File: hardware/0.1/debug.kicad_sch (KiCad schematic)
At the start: 11 parts, among them J401 JTAG, J402 JTAG, SW401 KMR2

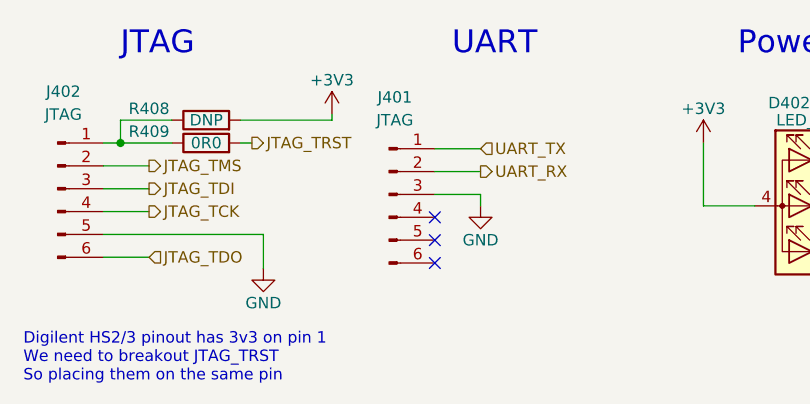
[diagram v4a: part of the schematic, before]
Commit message: usb3 routed less tuning
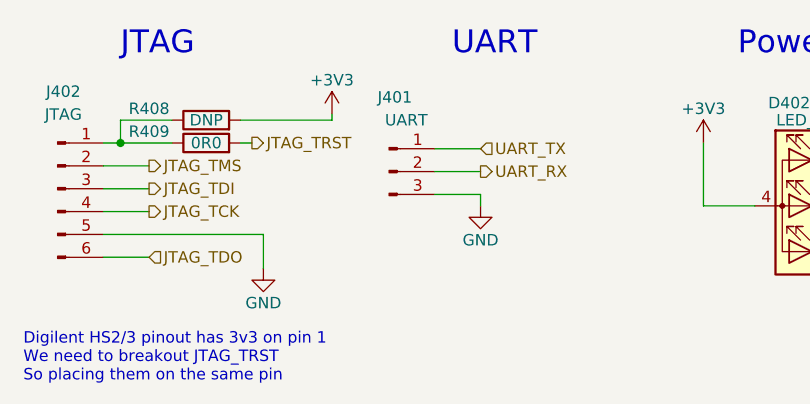
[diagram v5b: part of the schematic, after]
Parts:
- removed J401: JTAG, Connector:Tag-Connect_TC2030-IDC-NL_2x03_P1.27mm_Vertical, symbol Connector:Conn_01x06_Male
- added J401: UART, josh-connectors:3_PIN_THT_Staggered, symbol Connector:Conn_01x03_Male
- J402: footprint Connector:Tag-Connect_TC2030-IDC-NL_2x03_P1.27mm_Vertical -> josh-connectors:6_PIN_THT_Staggered
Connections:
- net GND: now also J401.3 (Pin_3)
- net UART_RX: now also J401.2 (Pin_2)
- net UART_TX: now also J401.1 (Pin_1)
- no-connect marks 3 -> 0
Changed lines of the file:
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@@
   (junction (at 74.295 98.425) (diameter 0) (color 0 0 0 0)
   )
-  (no_connect (at 160.02 98.425))
-  (no_connect (at 160.02 100.965))
-  (no_connect (at 160.02 103.505))
   (wire (pts (xy 128.27 102.87) (xy 123.19 102.87))
     (stroke (width 0) (type default) (color 0 0 0 0))
@@
     (property "Reference" "J402" (id 0) (at 118.745 84.455 0))
     (property "Value" "JTAG" (id 1) (at 118.745 86.995 0))
-    (property "Footprint" "Connector:Tag-Connect_TC2030-IDC-NL_2x03_P1.27mm_Vertical" (id 2) (at 118.11 95.25 0)
+    (property "Footprint" "josh-connectors:6_PIN_THT_Staggered" (id 2) (at 118.11 95.25 0)
       (effects (font (size 1.27 1.27)) hide)
     )
@@
     (pin "1")
   )
+  (symbol (lib_id "Connector:Conn_01x03_Male") (at 154.94 93.345 0) (unit 1)
+    (in_bom yes) (on_board yes)
+    (property "Reference" "J401" (id 0) (at 155.575 85.09 0))
+    (property "Value" "UART" (id 1) (at 156.845 87.63 0))
+    (property "Footprint" "josh-connectors:3_PIN_THT_Staggered" (id 2) (at 154.94 93.345 0)
+      (effects (font (size 1.27 1.27)) hide)
+    )
+    (property "Datasheet" "~" (id 3) (at 154.94 93.345 0)
+      (effects (font (size 1.27 1.27)) hide)
+    )
+    (pin "1")
+    (pin "2")
+    (pin "3")
+  )
   (symbol (lib_id "Device:R") (at 134.62 90.17 90) (unit 1)
     (in_bom yes) (on_board yes)
@@
     (pin "2")
   )
-  (symbol (lib_id "Connector:Conn_01x06_Male") (at 154.94 95.885 0) (unit 1)
-    (in_bom no) (on_board yes) (fields_autoplaced)
-    (property "Reference" "J401" (id 0) (at 155.575 85.09 0))
-    (property "Value" "JTAG" (id 1) (at 155.575 87.63 0))
-    (property "Footprint" "Connector:Tag-Connect_TC2030-IDC-NL_2x03_P1.27mm_Vertical" (id 2) (at 154.94 95.885 0)
-      (effects (font (size 1.27 1.27)) hide)
-    )
-    (property "Datasheet" "~" (id 3) (at 154.94 95.885 0)
-      (effects (font (size 1.27 1.27)) hide)
-    )
-    (pin "1")
-    (pin "2")
-    (pin "3")
-    (pin "4")
-    (pin "5")
-    (pin "6")
-  )
   (symbol (lib_id "power:GND") (at 76.835 107.95 0) (unit 1)

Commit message: wip, switchers todo
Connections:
- net GND: now also J401.1 (Pin_1); no longer J401.3 (Pin_3)
- net UART_TX: now also J401.3 (Pin_3); no longer J401.1 (Pin_1)
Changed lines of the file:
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@@
     (pin "1")
   )
-  (symbol (lib_id "Connector:Conn_01x03_Male") (at 154.94 93.345 0) (unit 1)
+  (symbol (lib_id "Connector:Conn_01x03_Male") (at 154.94 93.345 0) (mirror x) (unit 1)
     (in_bom yes) (on_board yes)
-    (property "Reference" "J401" (id 0) (at 155.575 85.09 0))
+    (property "Reference" "J401" (id 0) (at 156.845 85.725 0))
     (property "Value" "UART" (id 1) (at 156.845 87.63 0))
     (property "Footprint" "josh-connectors:3_PIN_THT_Staggered" (id 2) (at 154.94 93.345 0)

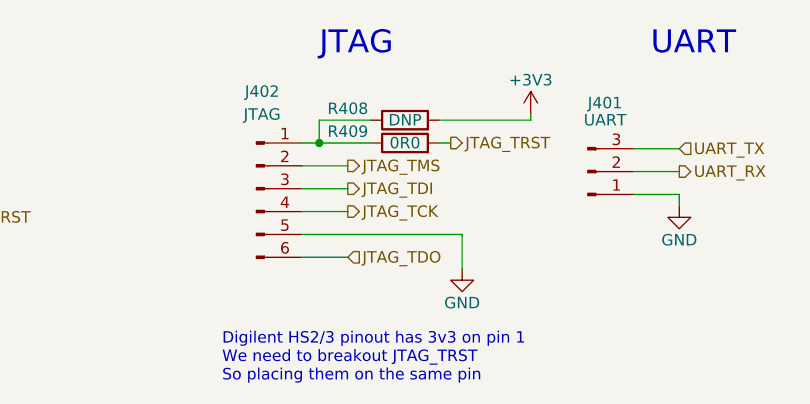
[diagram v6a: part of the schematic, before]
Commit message: erc = drc = 0, fixup BOM
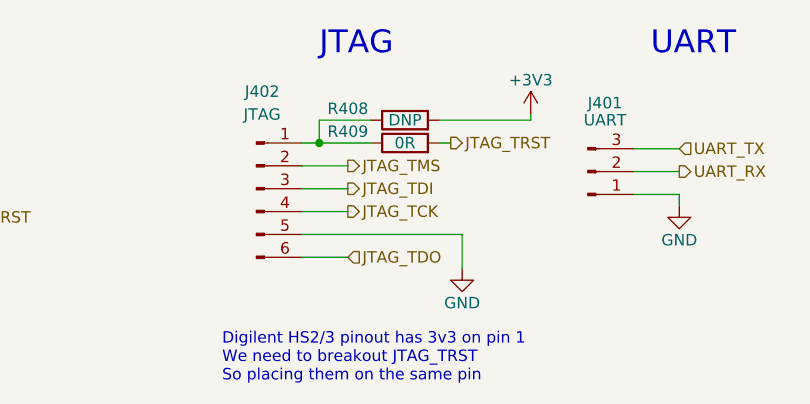
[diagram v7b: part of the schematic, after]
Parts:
- J401: now left out of the parts list
- R409: value 0R0 -> 0R; LCSC (none) -> C106231; MPN (none) -> C106231; Manufacturer (none) -> C106231
- SW401: LCSC (none) -> C2689601; MPN (none) -> KMR233GLFG; Manufacturer (none) -> C&K
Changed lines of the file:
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@@
   )
   (symbol (lib_id "Connector:Conn_01x03_Male") (at 154.94 93.345 0) (mirror x) (unit 1)
-    (in_bom yes) (on_board yes)
+    (in_bom no) (on_board yes)
     (property "Reference" "J401" (id 0) (at 156.845 85.725 0))
     (property "Value" "UART" (id 1) (at 156.845 87.63 0))
@@
     (in_bom yes) (on_board yes)
     (property "Reference" "R409" (id 0) (at 128.27 88.9 90))
-    (property "Value" "0R0" (id 1) (at 134.62 90.17 90))
+    (property "Value" "0R" (id 1) (at 134.62 90.17 90))
     (property "Footprint" "Resistor_SMD:R_0402_1005Metric" (id 2) (at 134.62 91.948 90)
       (effects (font (size 1.27 1.27)) hide)
     )
     (property "Datasheet" "~" (id 3) (at 134.62 90.17 0)
+      (effects (font (size 1.27 1.27)) hide)
+    )
+    (property "LCSC" "C106231" (id 4) (at 134.62 90.17 0)
+      (effects (font (size 1.27 1.27)) hide)
+    )
+    (property "MPN" "C106231" (id 5) (at 134.62 90.17 0)
+      (effects (font (size 1.27 1.27)) hide)
+    )
+    (property "Manufacturer" "C106231" (id 6) (at 134.62 90.17 0)
       (effects (font (size 1.27 1.27)) hide)
     )
@@
       (effects (font (size 1.27 1.27)) hide)
     )
-    (property "LCSC" "" (id 4) (at 64.77 98.425 0)
+    (property "LCSC" "C2689601" (id 4) (at 64.77 98.425 0)
       (effects (font (size 1.27 1.27)) hide)
     )
-    (property "MPN" "" (id 5) (at 64.77 98.425 0)
+    (property "MPN" "KMR233GLFG" (id 5) (at 64.77 98.425 0)
       (effects (font (size 1.27 1.27)) hide)
     )
-    (property "Manufacturer" "" (id 6) (at 64.77 98.425 0)
+    (property "Manufacturer" "C&K" (id 6) (at 64.77 98.425 0)
       (effects (font (size 1.27 1.27)) hide)
     )

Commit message: component shortage changes
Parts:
- R409: MPN C106231 -> RC0402FR-070RL
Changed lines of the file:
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@@
       (effects (font (size 1.27 1.27)) hide)
     )
-    (property "MPN" "C106231" (id 5) (at 134.62 90.17 0)
+    (property "MPN" "RC0402FR-070RL" (id 5) (at 134.62 90.17 0)
       (effects (font (size 1.27 1.27)) hide)
     )
